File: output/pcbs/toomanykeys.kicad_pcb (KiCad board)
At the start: 2 copper layers, 156 x 116.5 mm, 82 parts

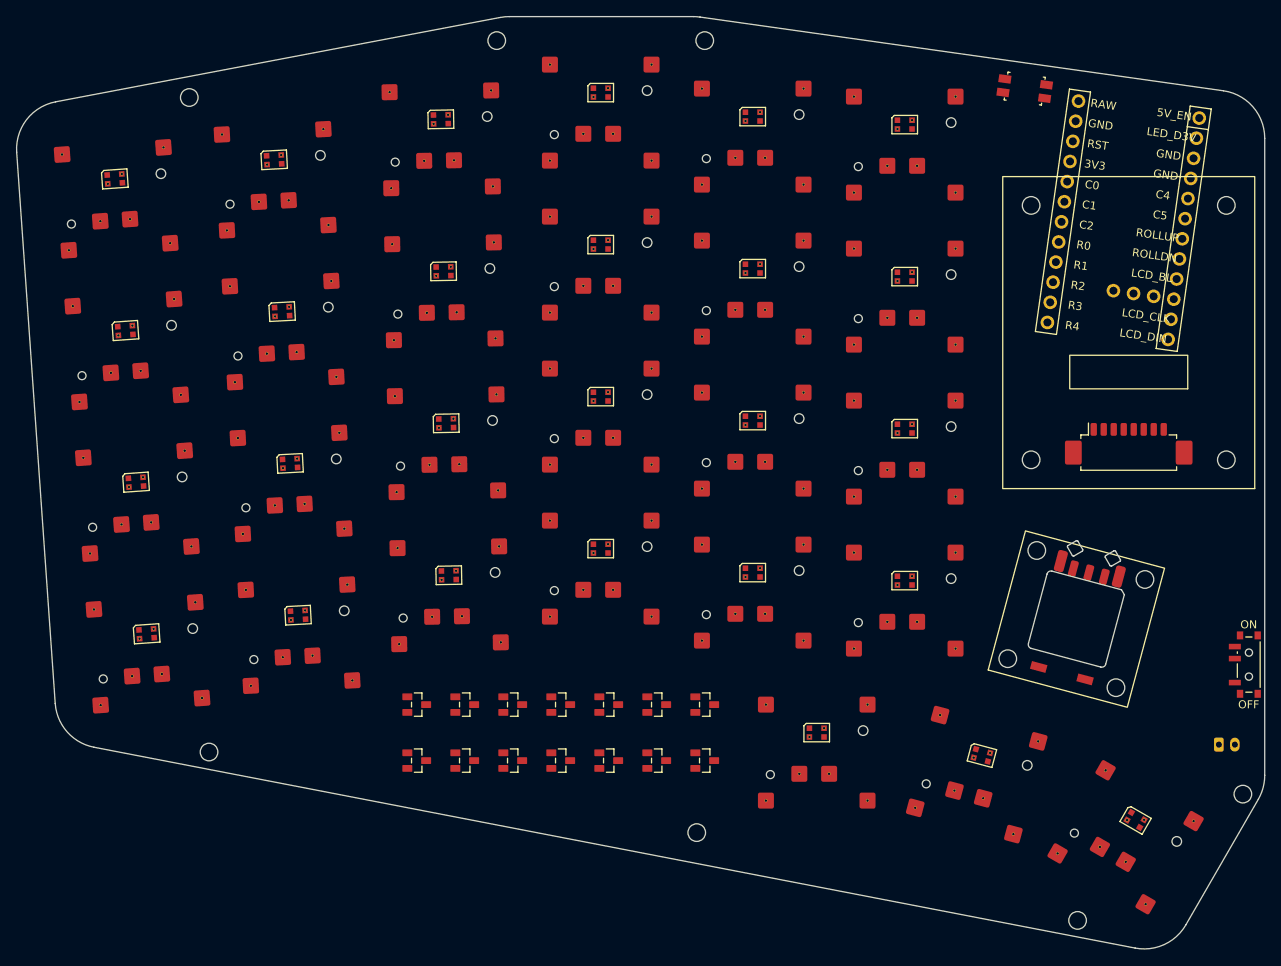
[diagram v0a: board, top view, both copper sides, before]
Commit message: Finish schematic. Partial routing draft. Minor changes to via sizes in ergogen.
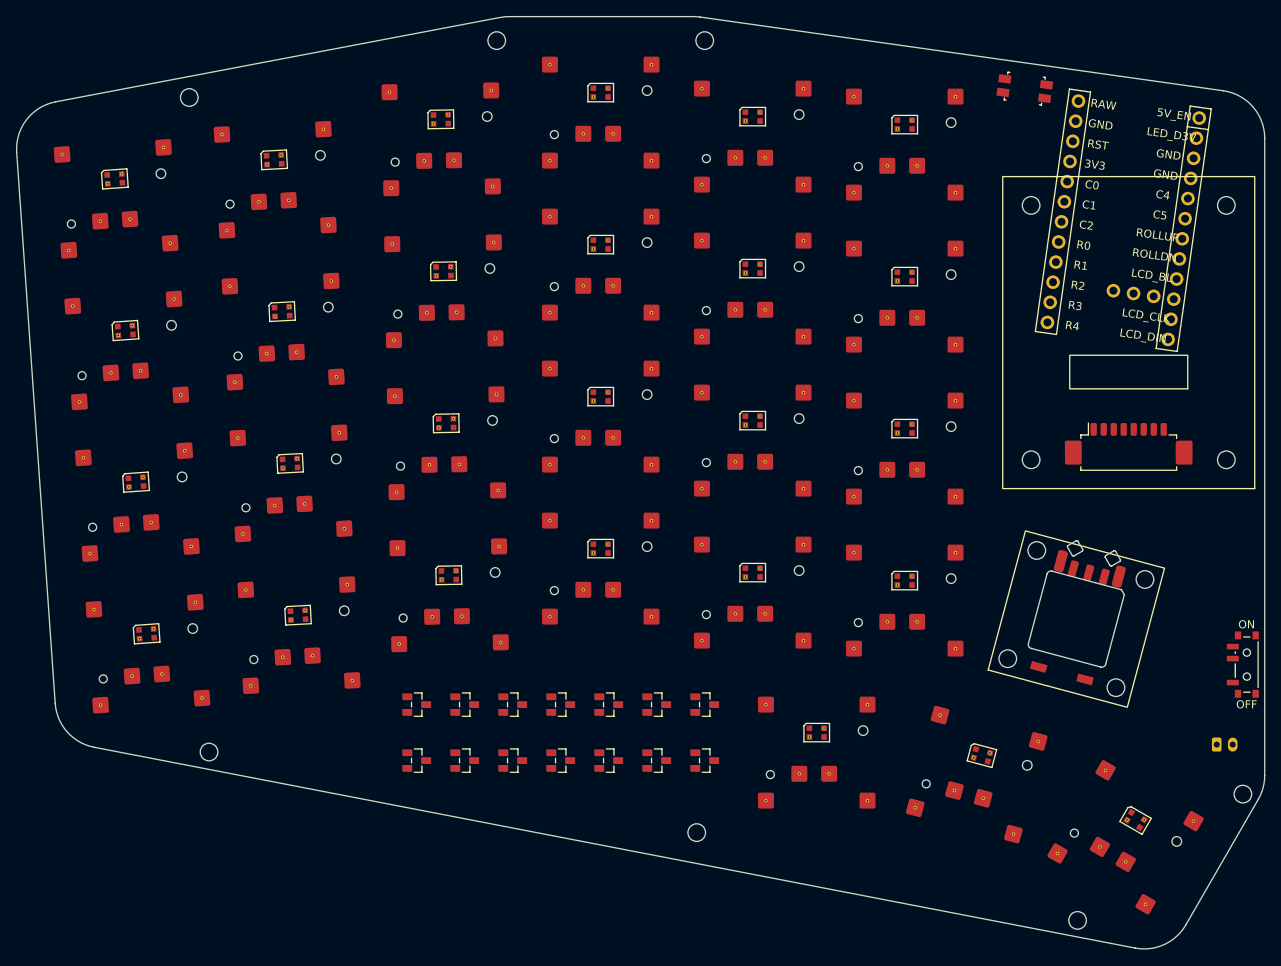
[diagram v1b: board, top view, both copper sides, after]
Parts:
- moved JST1 0.27 mm to (194.6, 171.4)
- moved PWR1 0.25 mm to (197.3, 161.4)
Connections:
- D14 pad 1: thumb_mid_fan -> thumb_far_fan
- D14 pad 2: thumb_far_fan -> thumb_mid_fan
- D2 pad 1: finger_middle_num -> finger_ring_num
- D2 pad 2: finger_ring_num -> finger_middle_num
- D3 pad 1: finger_inner_num -> finger_index_num
- D3 pad 2: finger_index_num -> finger_inner_num
- D5 pad 1: finger_middle_top -> finger_ring_top
- D5 pad 2: finger_ring_top -> finger_middle_top
- D6 pad 1: finger_inner_top -> finger_index_top
- D6 pad 2: finger_index_top -> finger_inner_top
- D8 pad 1: finger_middle_home -> finger_ring_home
- D8 pad 2: finger_ring_home -> finger_middle_home
- D9 pad 1: finger_inner_home -> finger_index_home
- D9 pad 2: finger_index_home -> finger_inner_home

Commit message: Finish clean routing. Attempted sync of schematic failed, but board LGTM and passes DRC other than CKW12 edge issues of no concern.
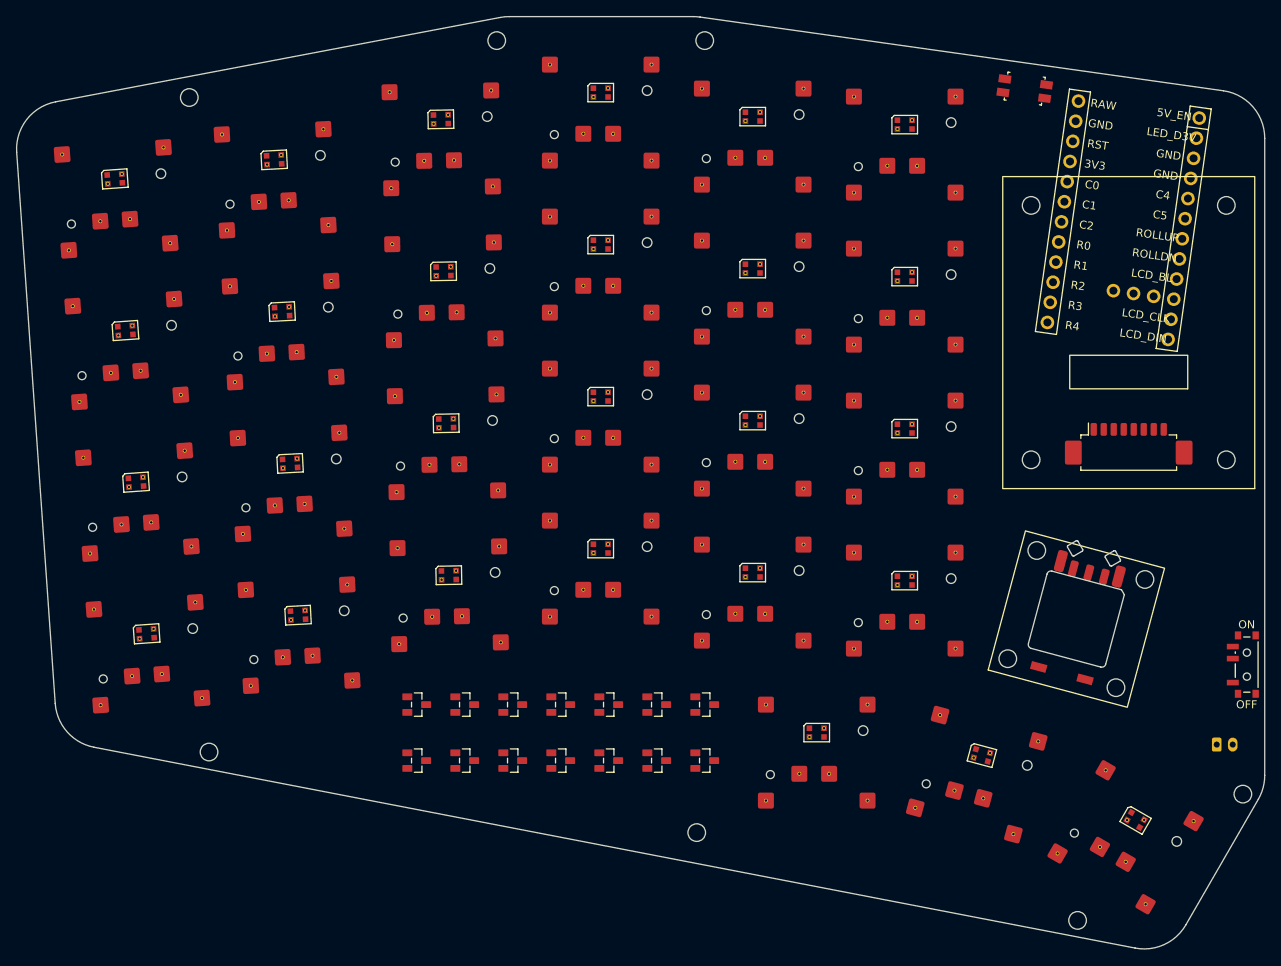
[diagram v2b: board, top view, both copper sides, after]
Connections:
- D12 pad 1: finger_inner_bottom -> finger_index_bottom
- D12 pad 2: finger_index_bottom -> finger_inner_bottom
- D14 pad 1: thumb_far_fan -> thumb_mid_fan
- D14 pad 2: thumb_mid_fan -> thumb_far_fan

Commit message: Successfully sync schematic and PCB for left halfgit add .git add .git add .!
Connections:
- D1 pad 1: finger_pinky_num -> finger_outer_num
- D1 pad 2: finger_outer_num -> finger_pinky_num
- D4 pad 1: finger_pinky_top -> finger_outer_top
- D4 pad 2: finger_outer_top -> finger_pinky_top
- D7 pad 1: finger_pinky_home -> finger_outer_home
- D7 pad 2: finger_outer_home -> finger_pinky_home
- MCU1 pad 10: LCD_DC -> LCD_DIN
- MCU1 pad 11: LCD_CLK -> ROLLUP
- MCU1 pad 12: LCD_DIN -> ROLLDN
- MCU1 pad 7: ROLLUP -> LCD_BL
- MCU1 pad 8: ROLLDN -> LCD_DC
- MCU1 pad 9: LCD_BL -> LCD_CLK
- S1 pad : GND -> (no net)
- S10 pad : GND -> (no net)
- S11 pad : GND -> (no net)
- S12 pad : GND -> (no net)
- S13 pad : GND -> (no net)
- S14 pad : GND -> (no net)
- S15 pad : GND -> (no net)
- S16 pad : GND -> (no net)
- S17 pad : GND -> (no net)
- S18 pad : GND -> (no net)
- S19 pad : GND -> (no net)
- S2 pad : GND -> (no net)
- S20 pad : GND -> (no net)
- S21 pad : GND -> (no net)
- S22 pad : GND -> (no net)
- S23 pad : GND -> (no net)
- S24 pad : GND -> (no net)
- S25 pad : GND -> (no net)
- S26 pad : GND -> (no net)
- S27 pad : GND -> (no net)
- S3 pad : GND -> (no net)
- S4 pad : GND -> (no net)
- S5 pad : GND -> (no net)
- S6 pad : GND -> (no net)
- S7 pad : GND -> (no net)
- S8 pad : GND -> (no net)
- S9 pad : GND -> (no net)
